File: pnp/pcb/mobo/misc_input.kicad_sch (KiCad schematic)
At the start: 26 parts, among them J2 X_LIMIT, J3 Y_LIMIT, J4 Z_LIMIT, J5 L_LIMIT, J6 R_LIMIT, J7 A_LIMIT, U2 TL072, U3 XGZP101SB1, U4 2SMPP-03, U5 XGZP101SB1, U6 2SMPP-03, U7 INA128, U8 INA128, U9 MCP3426-xMS

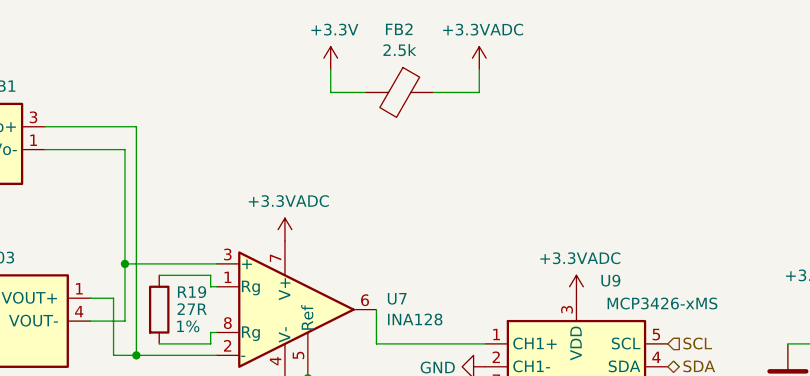
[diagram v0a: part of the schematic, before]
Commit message: Clean the ERC
- Changed some broken symbol links
- Changed all _Limit netlabels to _LIMIT

ERC list is now empty.
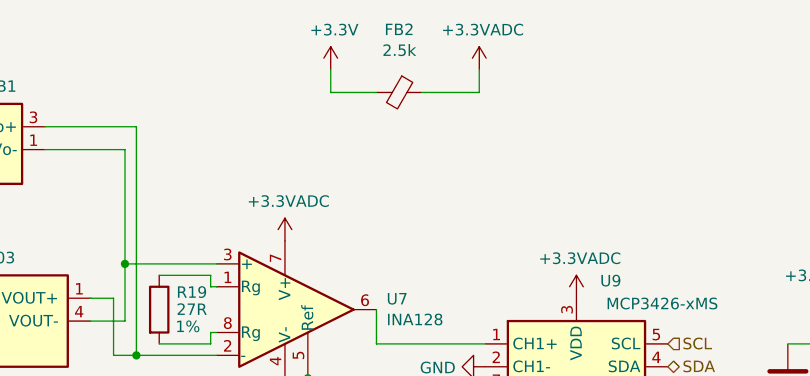
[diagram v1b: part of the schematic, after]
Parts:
- FB2: symbol Device:Ferrite_Bead -> Device:FerriteBead_Small
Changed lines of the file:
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@@
     (stroke (width 0) (type default) (color 0 0 0 0))
   )
-  (wire (pts (xy 210.82 69.85) (xy 205.74 69.85))
+  (wire (pts (xy 210.82 69.85) (xy 204.47 69.85))
     (stroke (width 0) (type default) (color 0 0 0 0))
   )
@@
     (stroke (width 0) (type default) (color 0 0 0 0))
   )
-  (wire (pts (xy 194.31 69.85) (xy 198.12 69.85))
+  (wire (pts (xy 194.31 69.85) (xy 199.39 69.85))
     (stroke (width 0) (type default) (color 0 0 0 0))
   )
@@
     (pin "1")
   )
-  (symbol (lib_id "Device:Ferrite_Bead") (at 201.93 69.85 270) (unit 1)
+  (symbol (lib_id "Device:FerriteBead_Small") (at 201.93 69.85 270) (unit 1)
     (in_bom yes) (on_board yes)
     (property "Reference" "FB2" (id 0) (at 201.93 62.8904 90))
